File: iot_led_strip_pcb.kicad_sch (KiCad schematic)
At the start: 38 parts, among them J1 I2C Expansion, J2 Conn_01x03_Socket, J3 GT-USB-7010ASV, J4 Barrel_Jack_Switch_Pin3Ring, J5 TC2050-IDC_Cortex-M, J6 Conn_01x03_Socket_Solderwire, Q1 BSS138, SW1 RESET, SW2 FLASH, U2 ESP32-S2-MINI-1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

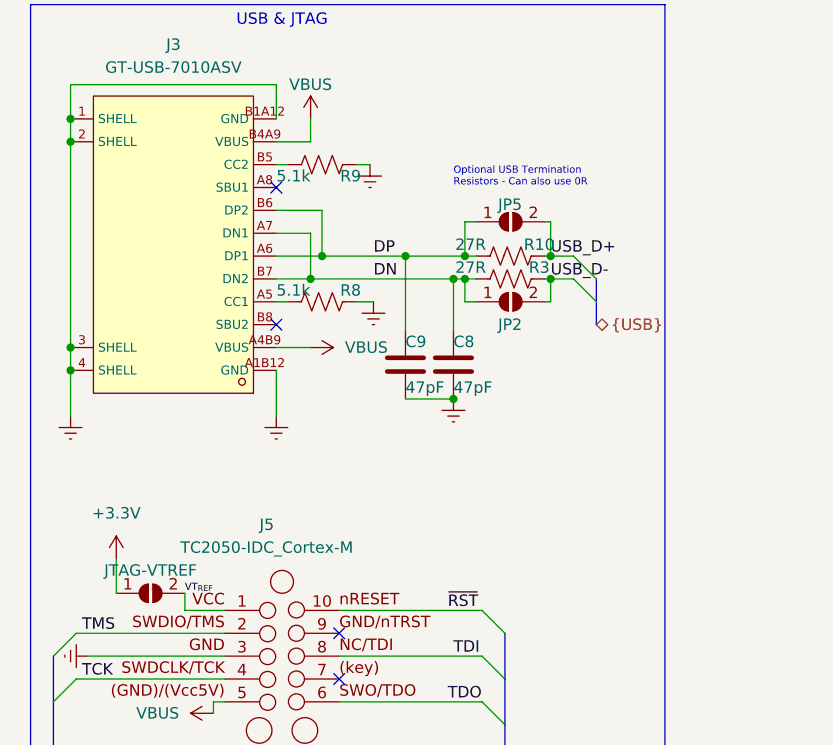
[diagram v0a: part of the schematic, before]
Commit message: some minor cleanup of schematic and layout
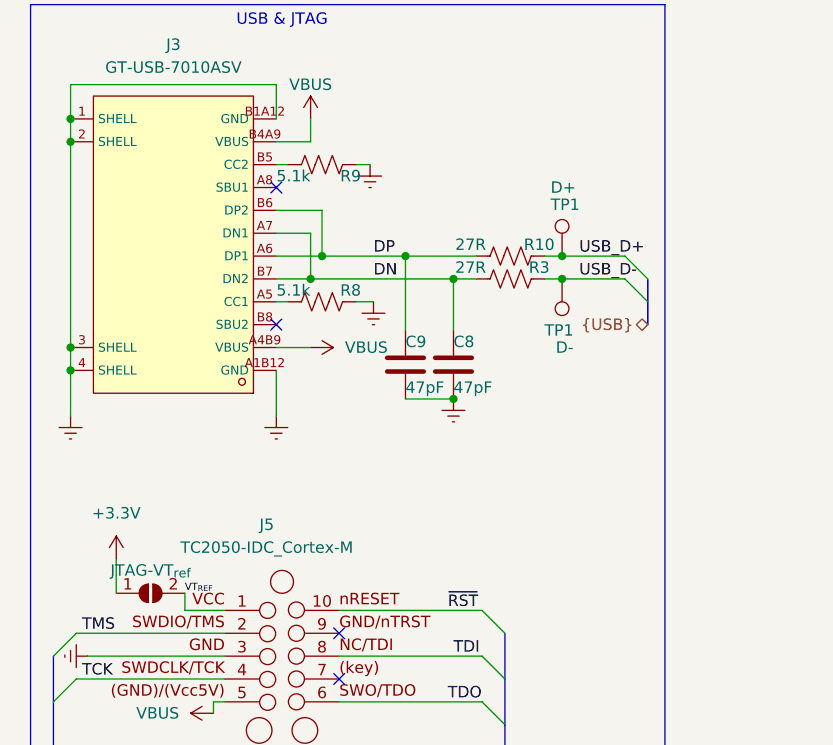
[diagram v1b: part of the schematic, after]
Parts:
- removed JP2, JP5: SolderJumper_2_Open, Jumper:SolderJumper-2_P1.3mm_Open_RoundedPad1.0x1.5mm, symbol Jumper:SolderJumper_2_Open
- added TP1: D+, TestPoint:TestPoint_Pad_D1.0mm, symbol Connector:TestPoint
- added TP1: D-, TestPoint:TestPoint_Pad_D1.0mm, symbol Connector:TestPoint
- JP2: value JTAG-VTREF -> JTAG-VT_{ref}
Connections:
- net USB_D+: now also TP1.1
- net USB_D-: now also TP1.1
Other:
- note removed: "Optional USB Termination Resistors - Can also use 0R"

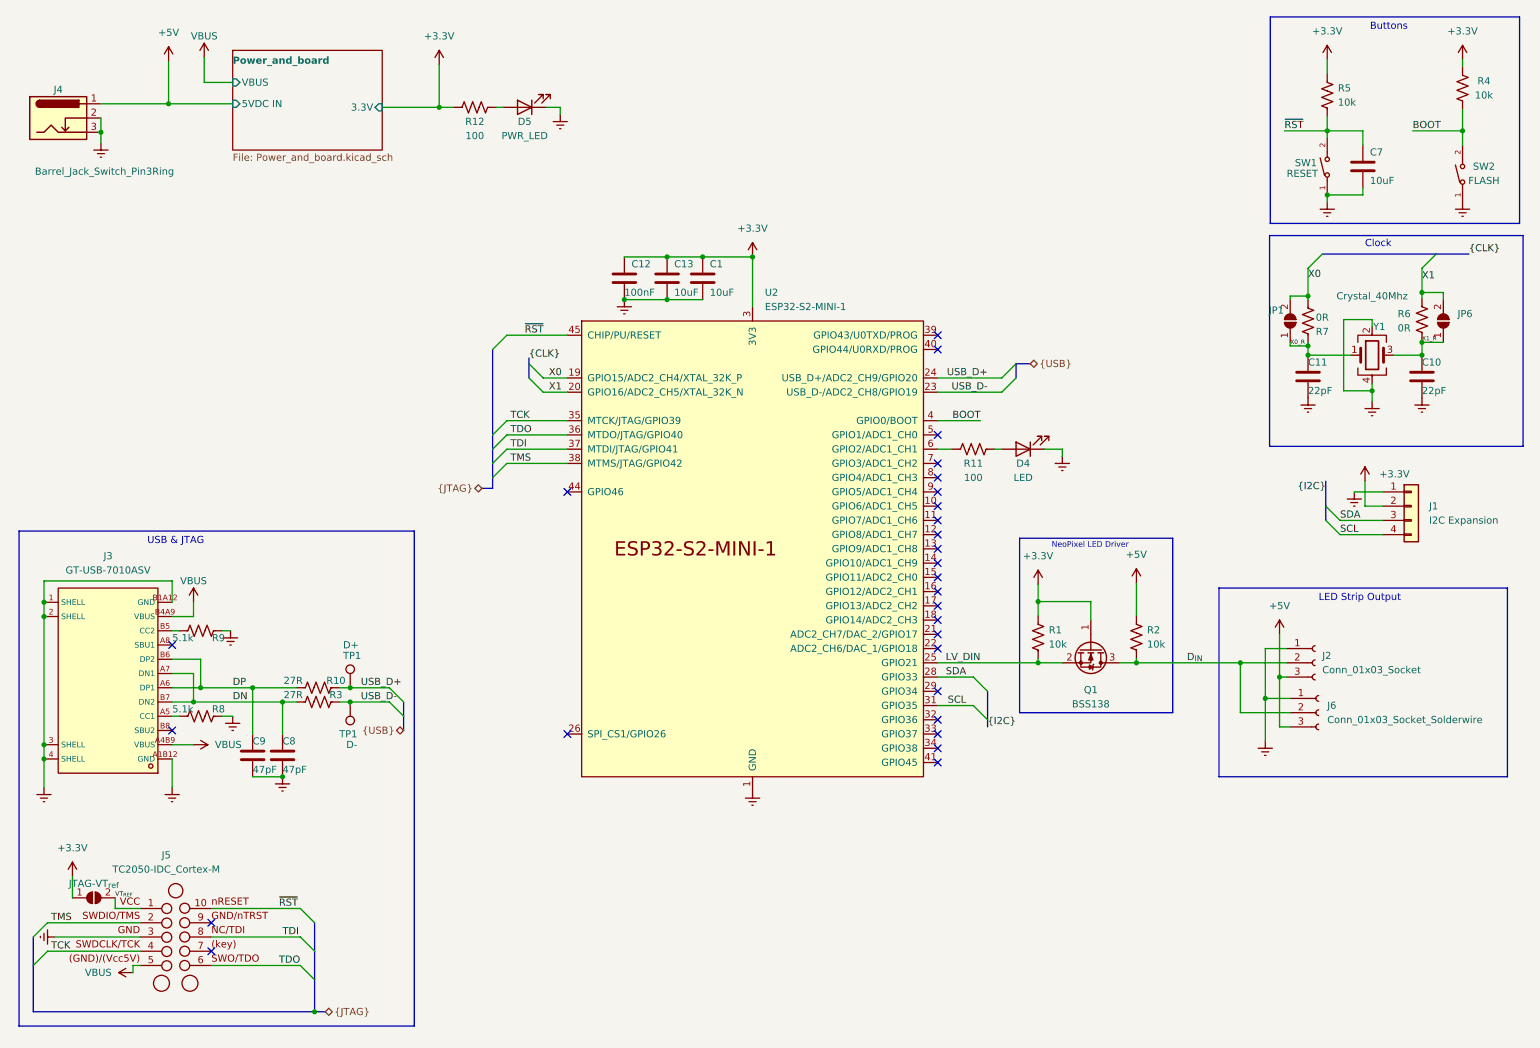
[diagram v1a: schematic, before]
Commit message: organized schematic & added bom
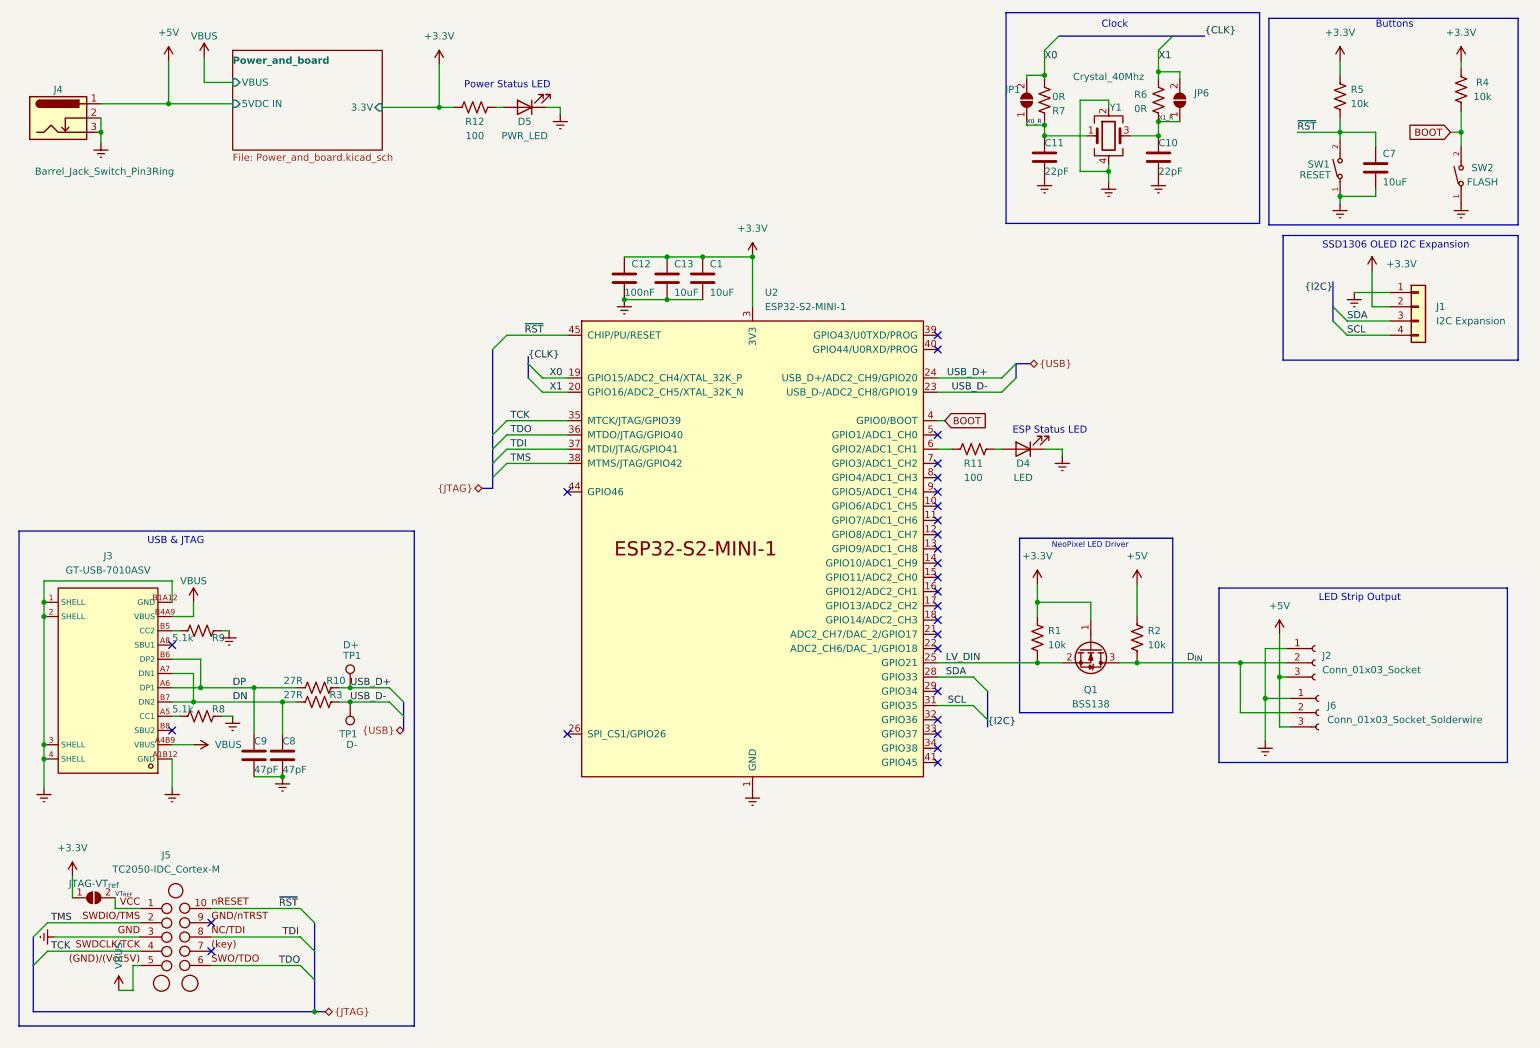
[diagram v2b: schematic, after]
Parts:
- C12: LCSC C15850 -> C49678; Vendor https://www.lcsc.com/product-detail/Multilayer-Ceramic-Capa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 -> https://jlcpcb.com/partdetail/Yageo-CC0805KRX7R9BB104/C49678
- J5, JP1, JP6: now left out of the parts list
- Q1: LCSC (none) -> C358381; Vendor (none) -> https://jlcpcb.com/partdetail/Foshan_Blue_RocketElec-BSS138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
- R11: Vendor https://www.lcsc.com/product-detail/Chip-Resistor-Surface-M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 -> https://jlcpcb.com/partdetail/18096-0805W8F1000T5E/C17408
- R12: LCSC C17710 -> C17408; Vendor https://www.lcsc.com/product-detail/Chip-Resistor-Surface-M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 -> https://jlcpcb.com/partdetail/18096-0805W8F1000T5E/C17408
- U2: LCSC (none) -> C3013906
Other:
- note added: "ESP Status LED"
- note added: "Power Status LED"
- note added: "SSD1306 OLED I2C Expansion"
- moved on the sheet: C10, C11, C7, J1, JP1, JP6, R5, R6, R7, SW1, Y1

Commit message: final modifications, cleanup, added v2.0 photos as ordered
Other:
- title: Spotify Reactive IoT LED Strip Driver -> Spotify Neopixel Visualizer
- moved on the sheet: J2, J6

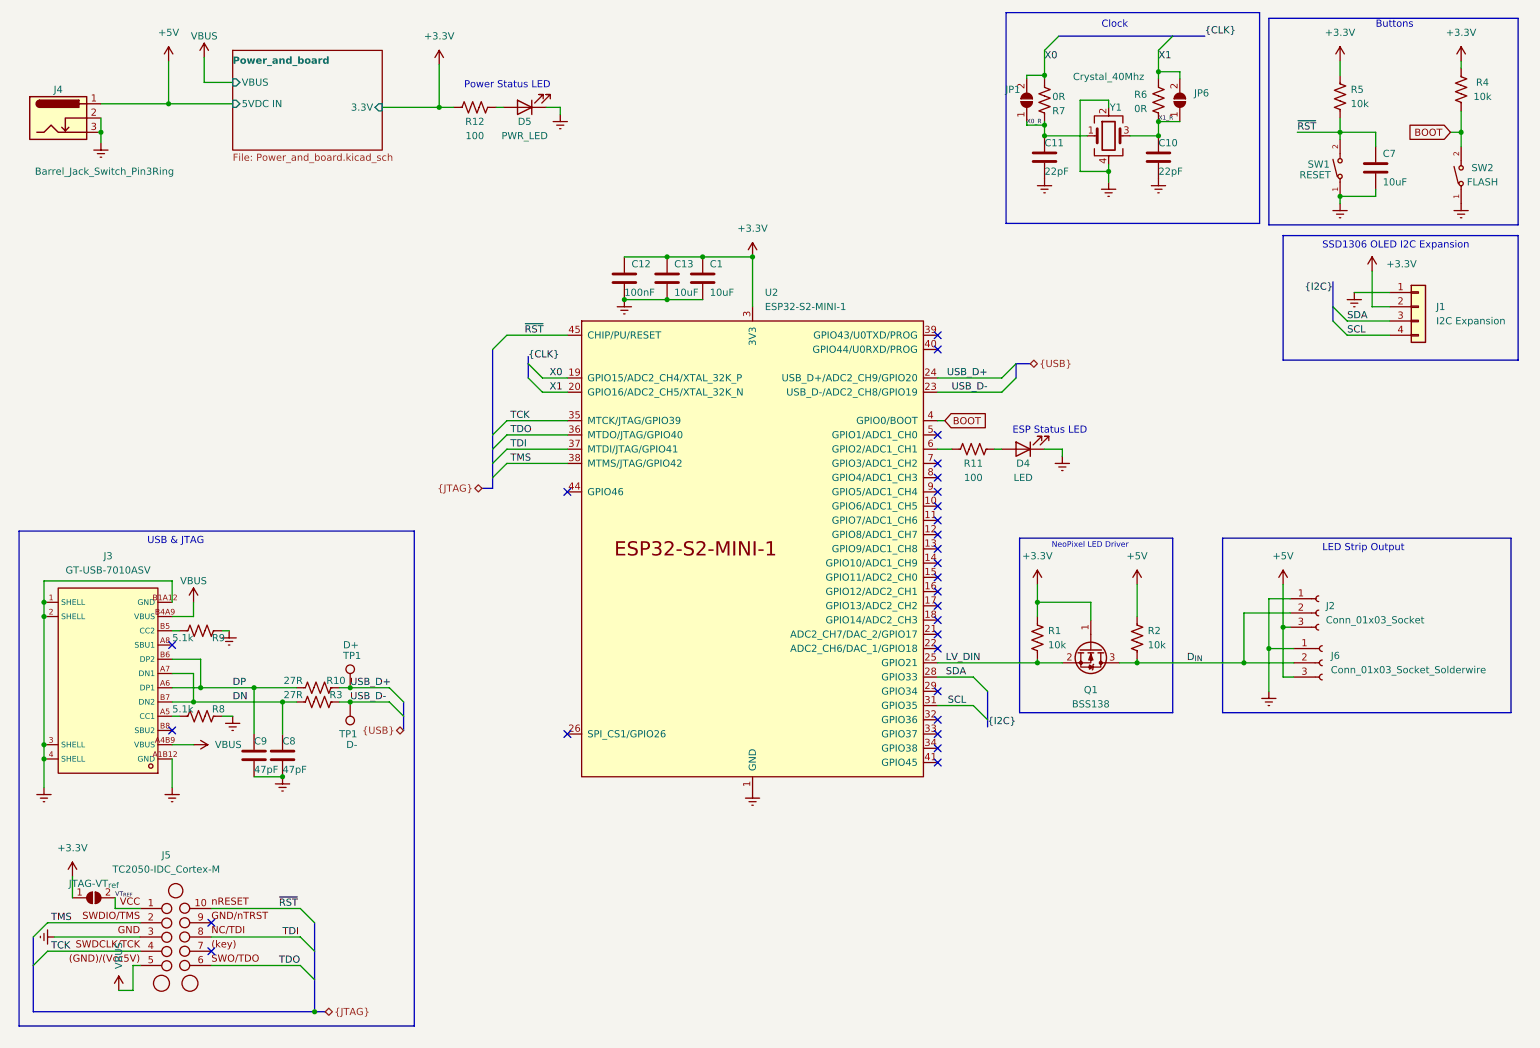
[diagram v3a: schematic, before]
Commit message: Moved button labels and multiple minor modifications
* Implemented Orion's suggestion for replacing 10uF cap on reset button
  with 100nF.
* Moved silkscreen for both buttons underneath and moved jtag label.
* Added labels to both power and status LEDs.
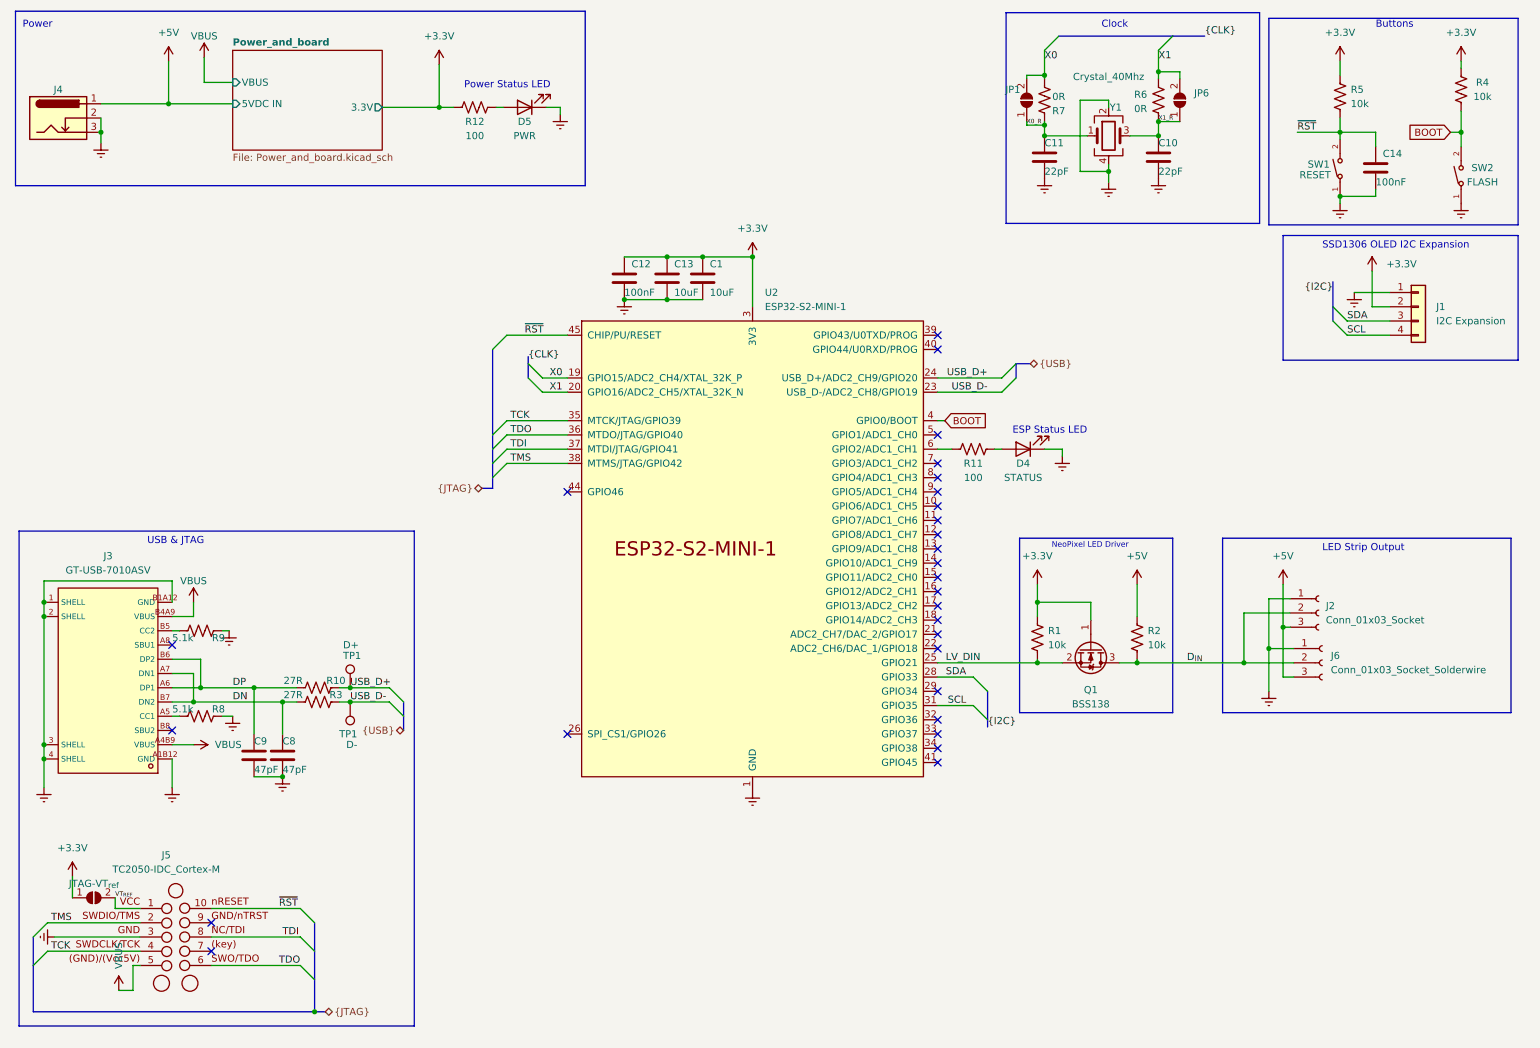
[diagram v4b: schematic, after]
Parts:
- removed C7: 10uF, Capacitor_SMD:C_0805_2012Metric_Pad1.18x1.45mm_HandSolder, symbol Device:C
- added C14: 100nF, Capacitor_SMD:C_0805_2012Metric_Pad1.18x1.45mm_HandSolder, symbol Device:C
- D4: value LED -> STATUS
- D5: value PWR_LED -> PWR
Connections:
- net Earth: now also C14.2
- net ~{RST}: now also C14.1
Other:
- note added: "Power"

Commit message: small modifications + RT render
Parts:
- D4: value STATUS -> STAT
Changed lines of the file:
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@@
       (effects (font (size 1.27 1.27)))
     )
-    (property "Value" "STATUS" (at 193.675 97.155 0)
+    (property "Value" "STAT" (at 193.675 97.155 0)
       (effects (font (size 1.27 1.27)))
     )
@@
   (sheet (at 52.705 20.955) (size 26.67 17.78) (fields_autoplaced)
     (stroke (width 0.1524) (type solid))
-    (fill (color 0 0 0 0.0000))
+    (fill (color 255 255 194 1.0000))
     (property "Sheetname" "Power_and_board" (at 52.705 20.2434 0)
       (effects (font (size 1.27 1.27) bold) (justify left bottom))
